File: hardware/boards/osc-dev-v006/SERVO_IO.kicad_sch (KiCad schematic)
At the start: 10 parts, among them J10 PIN-1-3P, J11 JST-PH-V, J9 PIN-1-3P, U4 74LVC2G241

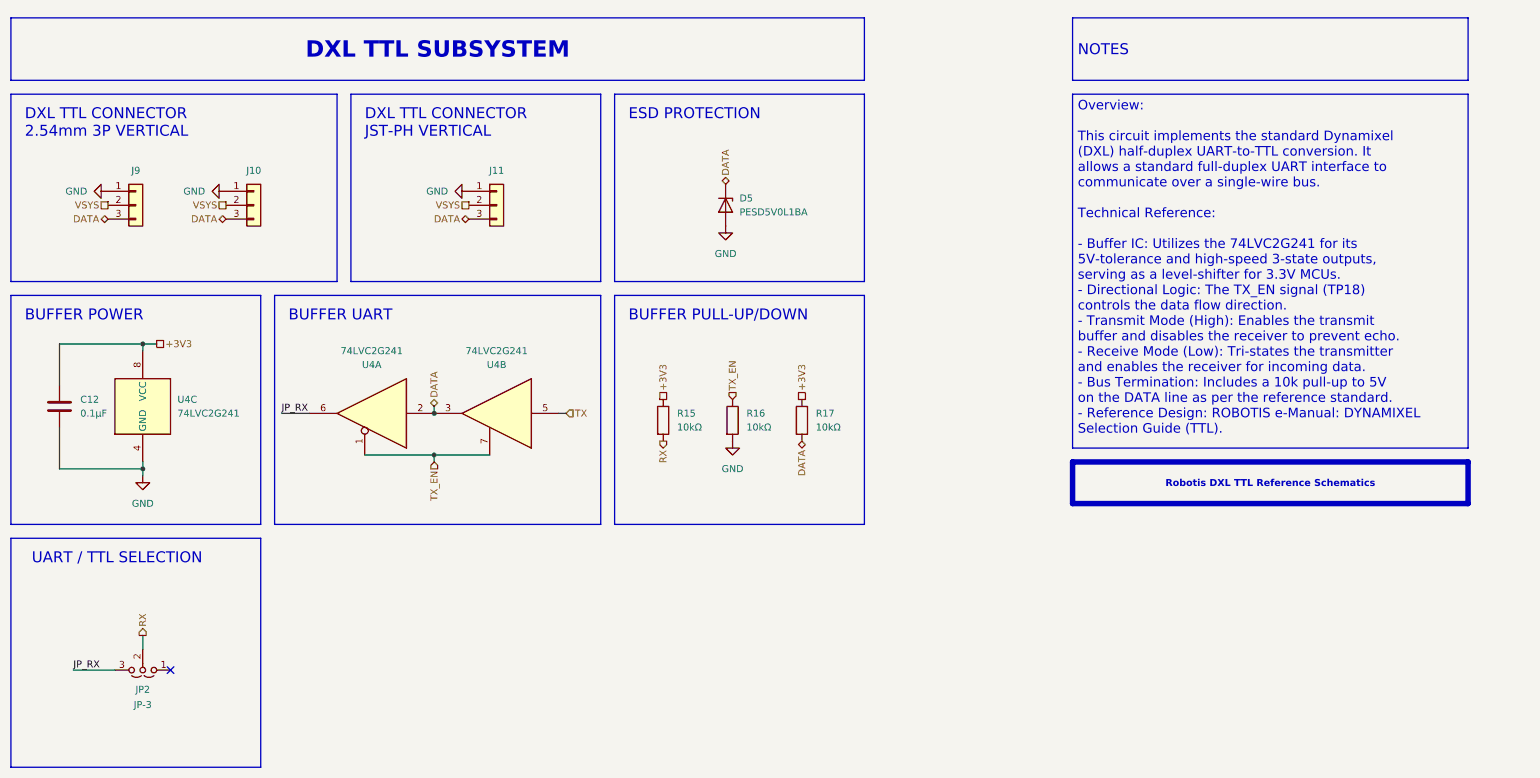
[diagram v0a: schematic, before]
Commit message: rename board to osc-dev-v006
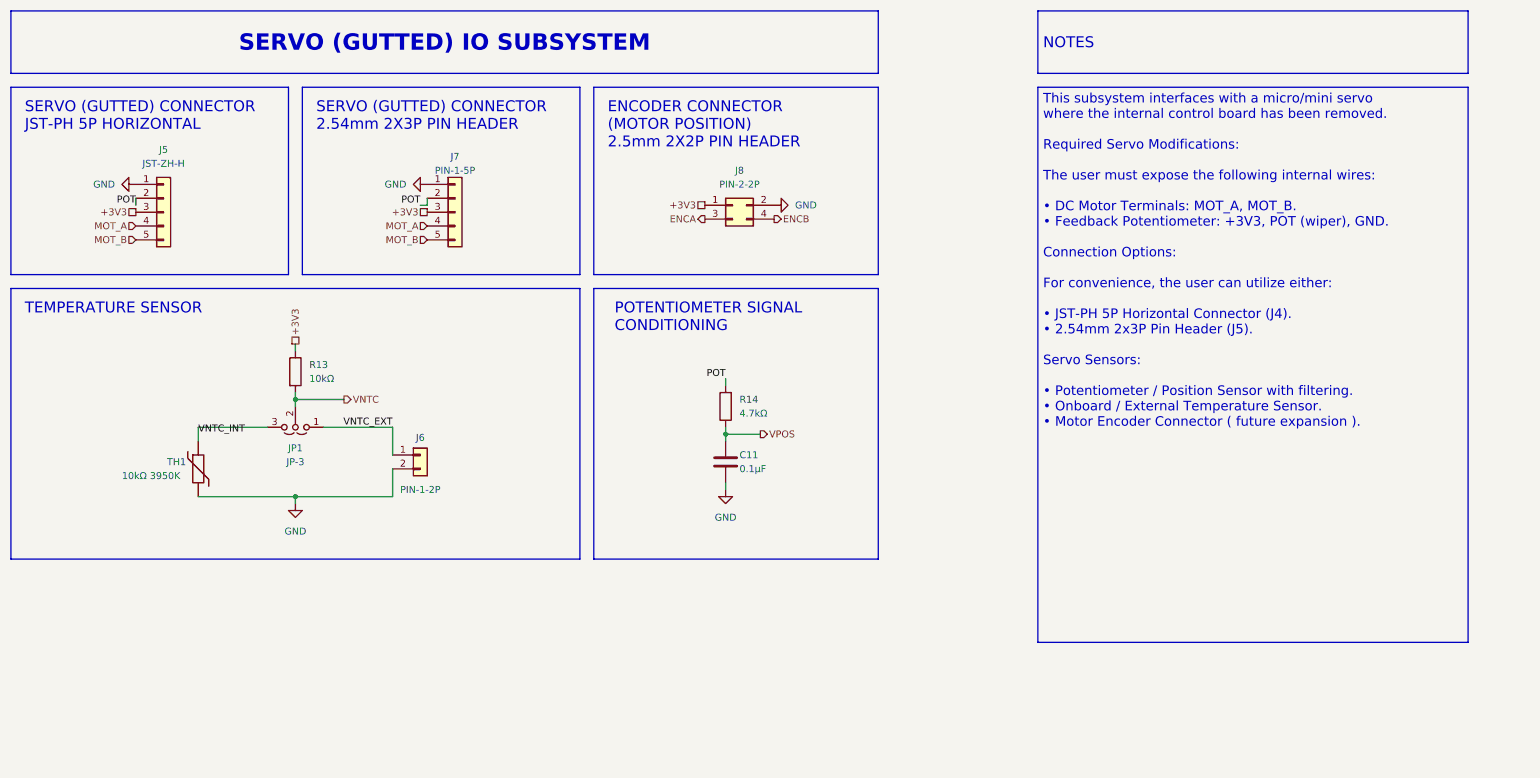
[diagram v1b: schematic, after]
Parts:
- removed C12: 0.1µF, Capacitor_SMD:C_0805_2012Metric_Pad1.18x1.45mm_HandSolder, symbol Device:C
- removed D5: PESD5V0L1BA, Diode_SMD:D_SOD-323_HandSoldering, symbol Diode:PESD5V0L1UL
- removed J10, J9: PIN-1-3P, Connector_PinHeader_2.54mm:PinHeader_1x03_P2.54mm_Vertical, symbol Connector_Generic:Conn_01x03
- removed J11: JST-PH-V, shared:CONN-TH_B3B-PH-K-S, symbol Connector_Generic:Conn_01x03
- removed JP2: JP-3, Connector_PinHeader_2.54mm:PinHeader_1x03_P2.54mm_Vertical, symbol Jumper:Jumper_3_Open
- removed R15, R16, R17: 10kΩ, Resistor_SMD:R_0805_2012Metric_Pad1.20x1.40mm_HandSolder, symbol Device:R
- removed U4: 74LVC2G241, shared:VSSOP-8_L2.3-W2.0-P0.50-LS3.1-BR, symbol 74xGxx:74LVC2G241
- added C11: 0.1µF, Capacitor_SMD:C_0805_2012Metric_Pad1.18x1.45mm_HandSolder, symbol Device:C
- added J5: JST-ZH-H, shared:CONN-TH_S5B-ZR-LF-SN, symbol Connector_Generic:Conn_01x05
- added J6: PIN-1-2P, Connector_PinHeader_2.54mm:PinHeader_1x02_P2.54mm_Vertical, symbol Connector_Generic:Conn_01x02
- added J7: PIN-1-5P, Connector_PinHeader_2.54mm:PinHeader_1x05_P2.54mm_Vertical, symbol Connector_Generic:Conn_01x05
- added J8: PIN-2-2P, Connector_PinHeader_2.54mm:PinHeader_2x02_P2.54mm_Vertical, symbol Connector_Generic:Conn_02x02_Odd_Even
- added JP1: JP-3, Connector_PinHeader_2.54mm:PinHeader_1x03_P2.54mm_Vertical, symbol Jumper:Jumper_3_Open
- added R13: 10kΩ, Resistor_SMD:R_0805_2012Metric_Pad1.20x1.40mm_HandSolder, symbol Device:R
- added R14: 4.7kΩ, Resistor_SMD:R_0805_2012Metric_Pad1.20x1.40mm_HandSolder, symbol Device:R
- added TH1: 10kΩ 3950K, Resistor_SMD:R_0805_2012Metric_Pad1.20x1.40mm_HandSolder, symbol Device:Thermistor
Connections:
- net +3V3: now also J5.3 (Pin_3), J7.3 (Pin_3), J8.1 (Pin_1), R13.1
- net GND: now also C11.2, J5.1 (Pin_1), J6.2 (Pin_2), J7.1 (Pin_1), J8.2 (Pin_2), TH1.2
- new net ENCA: J8.3 (Pin_3)
- new net ENCB: J8.4 (Pin_4)
- new net MOT_A: J5.4 (Pin_4), J7.4 (Pin_4)
- new net MOT_B: J5.5 (Pin_5), J7.5 (Pin_5)
- new net POT: J5.2 (Pin_2), J7.2 (Pin_2), R14.2
- new net VNTC: JP1.2 (C), R13.2
- new net VNTC_EXT: J6.1 (Pin_1), JP1.1 (A)
- new net VNTC_INT: JP1.3 (B), TH1.1
- new net VPOS: C11.1, R14.1
- no-connect marks 1 -> 0
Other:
- note added: "ENCODER CONNECTOR (MOTOR POSITION) 2.5mm 2X2P PIN HEADER"
- note added: "POTENTIOMETER SIGNAL CONDITIONING"
- note added: "SERVO (GUTTED) CONNECTOR 2.54mm 2X3P PIN HEADER"
- note added: "SERVO (GUTTED) CONNECTOR JST-PH 5P HORIZONTAL"
- note added: "TEMPERATURE SENSOR"
- note removed: "BUFFER POWER"
- note removed: "BUFFER PULL-UP/DOWN"
- note removed: "BUFFER UART"
- note removed: "DXL TTL CONNECTOR 2.54mm 3P VERTICAL"
- note removed: "DXL TTL CONNECTOR JST-PH VERTICAL"
- note removed: "ESD PROTECTION"
- note removed: "UART / TTL SELECTION"
